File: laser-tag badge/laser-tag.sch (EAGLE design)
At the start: 47 parts, among them J1 JUMPER_SOLDER_1X2_CLOSED, J2 JUMPER_SOLDER_1X2_OPEN, J3 JUMPER_SOLDER_1X2_CLOSED, J4 JUMPER_SOLDER_1X2_CLOSED, J5 JUMPER_SOLDER_1X2_CLOSED, P1 E1260CS021, U1 MKL27Z256VLH4

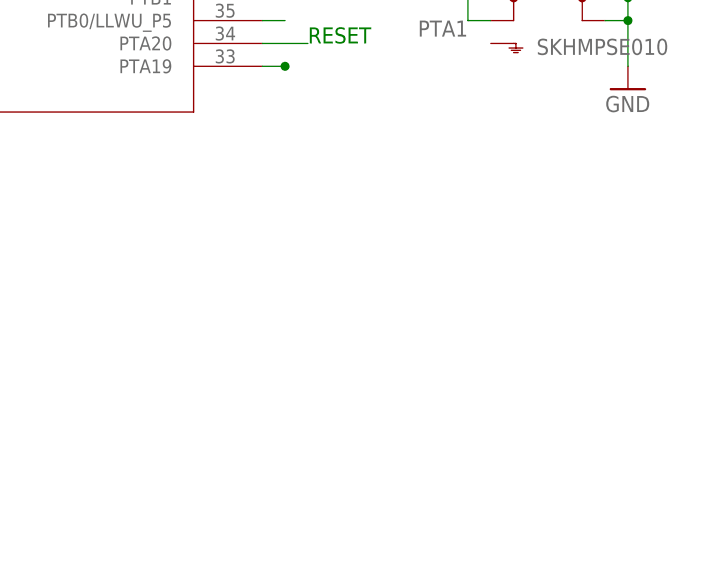
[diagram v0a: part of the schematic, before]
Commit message: Added fiducials
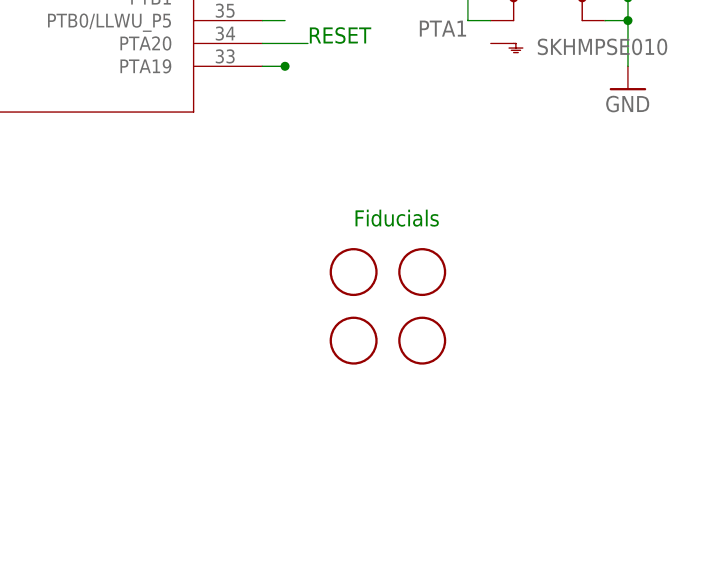
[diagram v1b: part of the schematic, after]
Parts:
- added U$1, U$2, U$3, U$4: FIDUCIAL, adafruit:FIDUCIAL
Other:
- note added: "Fiducials"
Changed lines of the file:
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@@
 <part name="BAT2" library="adafruit" deviceset="CR2032" device="SMT" value="BK-883"/>
 <part name="USB" library="SparkFun-Connectors" deviceset="USB" device="-MICROB" value="10104110-0001LF"/>
+<part name="U$1" library="adafruit" deviceset="FIDUCIAL" device=""/>
+<part name="U$2" library="adafruit" deviceset="FIDUCIAL" device=""/>
+<part name="U$3" library="adafruit" deviceset="FIDUCIAL" device=""/>
+<part name="U$4" library="adafruit" deviceset="FIDUCIAL" device=""/>
 </parts>
 <sheets>
@@
 <text x="-7.62" y="38.1" size="1.778" layer="91">SWD_DIO</text>
 <text x="121.92" y="22.86" size="1.778" layer="91">RESET</text>
+<text x="127" y="2.54" size="1.778" layer="91">Fiducials</text>
 </plain>
 <instances>
@@
 <instance part="BAT2" gate="G$1" x="-124.46" y="88.9" rot="R90"/>
 <instance part="USB" gate="G$1" x="-104.14" y="10.16" rot="R180"/>
+<instance part="U$1" gate="G$1" x="127" y="-2.54"/>
+<instance part="U$2" gate="G$1" x="134.62" y="-2.54"/>
+<instance part="U$3" gate="G$1" x="127" y="-10.16"/>
+<instance part="U$4" gate="G$1" x="134.62" y="-10.16"/>
 </instances>
 <busses>

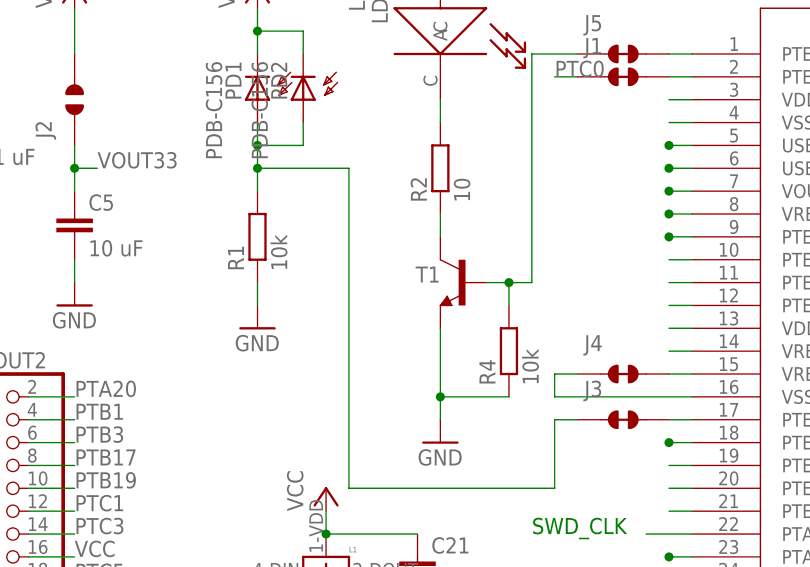
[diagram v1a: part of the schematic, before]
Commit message: Replace T1 with Q1
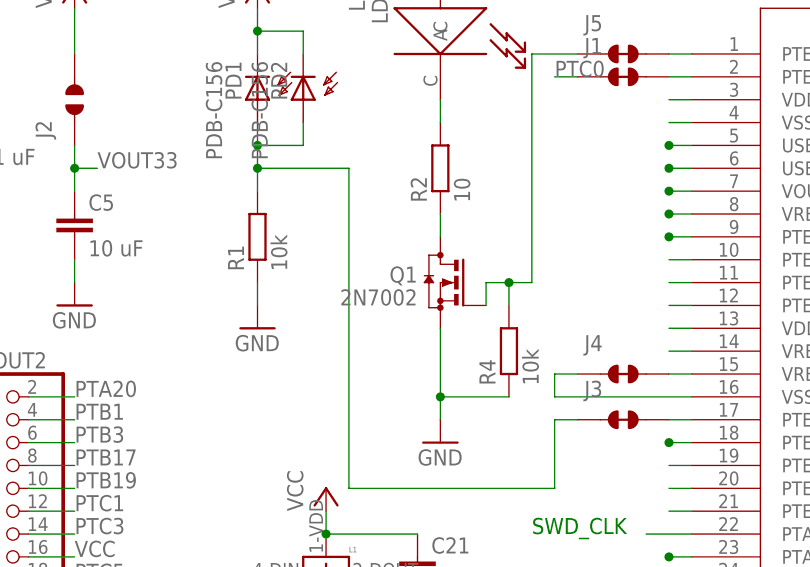
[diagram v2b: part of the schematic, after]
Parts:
- removed T1: (no value), transistor:BC850-NPN-SOT23-BEC
- added Q1: 2N7002, transistor-small-signal:BSS123
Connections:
- net GND: now also Q1.S; no longer T1.E
- net N$1: now also Q1.D; no longer T1.C
- net N$10: now also Q1.G; no longer T1.B
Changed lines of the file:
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@@
 <part name="LD1" library="Photonics" deviceset="LD" device=""/>
 <part name="P+1" library="supply1" deviceset="VCC" device=""/>
-<part name="T1" library="transistor" deviceset="*-NPN-" device="SOT23-BEC" technology="BC850"/>
 <part name="GND1" library="supply1" deviceset="GND" device=""/>
 <part name="P+2" library="supply1" deviceset="VCC" device=""/>
@@
 <part name="U$3" library="adafruit" deviceset="FIDUCIAL" device=""/>
 <part name="U$4" library="adafruit" deviceset="FIDUCIAL" device=""/>
+<part name="Q1" library="transistor-small-signal" deviceset="BSS123" device="" value="2N7002"/>
 </parts>
 <sheets>
@@
 <instance part="LD1" gate="A" x="-17.78" y="101.6" rot="R270"/>
 <instance part="P+1" gate="VCC" x="-17.78" y="114.3"/>
-<instance part="T1" gate="G$1" x="-15.24" y="73.66" smashed="yes" rot="MR0">
-<attribute name="NAME" x="-17.78" y="73.66" size="1.778" layer="95" rot="MR0"/>
-<attribute name="VALUE" x="-5.08" y="78.74" size="1.778" layer="96" rot="MR0"/>
-</instance>
 <instance part="GND1" gate="1" x="-17.78" y="55.88"/>
 <instance part="P+2" gate="VCC" x="-38.1" y="106.68"/>
@@
 <instance part="U$3" gate="G$1" x="127" y="-10.16"/>
 <instance part="U$4" gate="G$1" x="134.62" y="-10.16"/>
+<instance part="Q1" gate="G$1" x="-17.78" y="73.66" rot="MR0"/>
 </instances>
 <busses>
@@
 <segment>
 <pinref part="GND1" gate="1" pin="GND"/>
-<pinref part="T1" gate="G$1" pin="E"/>
 <wire x1="-17.78" y1="58.42" x2="-17.78" y2="60.96" width="0.1524" layer="91"/>
 <pinref part="R4" gate="G$1" pin="1"/>
@@
 <wire x1="-10.16" y1="60.96" x2="-17.78" y2="60.96" width="0.1524" layer="91"/>
 <junction x="-17.78" y="60.96"/>
+<pinref part="Q1" gate="G$1" pin="S"/>
 </segment>
 <segment>
@@
 <net name="N$1" class="0">
 <segment>
-<pinref part="T1" gate="G$1" pin="C"/>
 <pinref part="R2" gate="G$1" pin="1"/>
 <wire x1="-17.78" y1="78.74" x2="-17.78" y2="81.28" width="0.1524" layer="91"/>
+<pinref part="Q1" gate="G$1" pin="D"/>
 </segment>
 </net>
@@
 <net name="N$10" class="0">
 <segment>
-<pinref part="T1" gate="G$1" pin="B"/>
 <wire x1="-12.7" y1="73.66" x2="-10.16" y2="73.66" width="0.1524" layer="91"/>
 <wire x1="-10.16" y1="73.66" x2="-7.62" y2="73.66" width="0.1524" layer="91"/>
@@
 <wire x1="-10.16" y1="71.12" x2="-10.16" y2="73.66" width="0.1524" layer="91"/>
 <junction x="-10.16" y="73.66"/>
-</segment>
-</net>
+<pinref part="Q1" gate="G$1" pin="G"/>
+<wire x1="-12.7" y1="71.12" x2="-12.7" y2="73.66" width="0.1524" layer="91"/>
+</segment>
+</net>

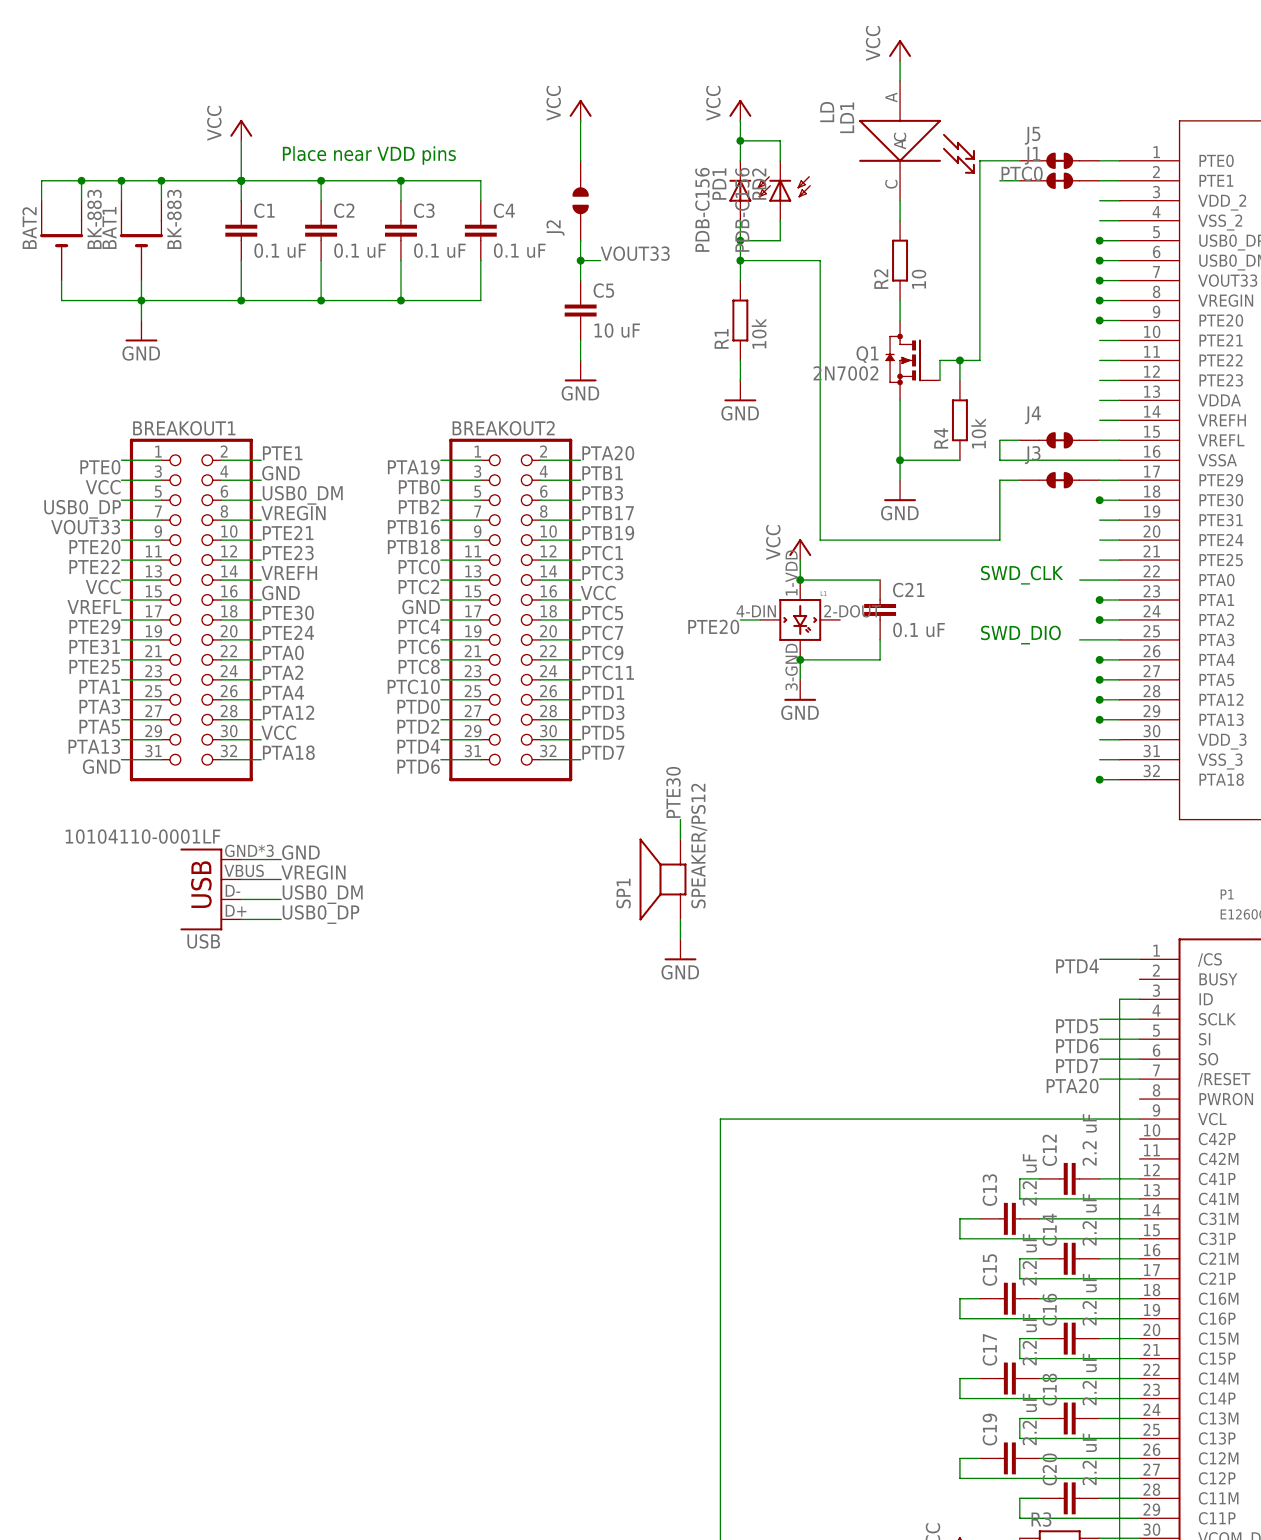
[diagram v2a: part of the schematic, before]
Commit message: Battery protection circuit
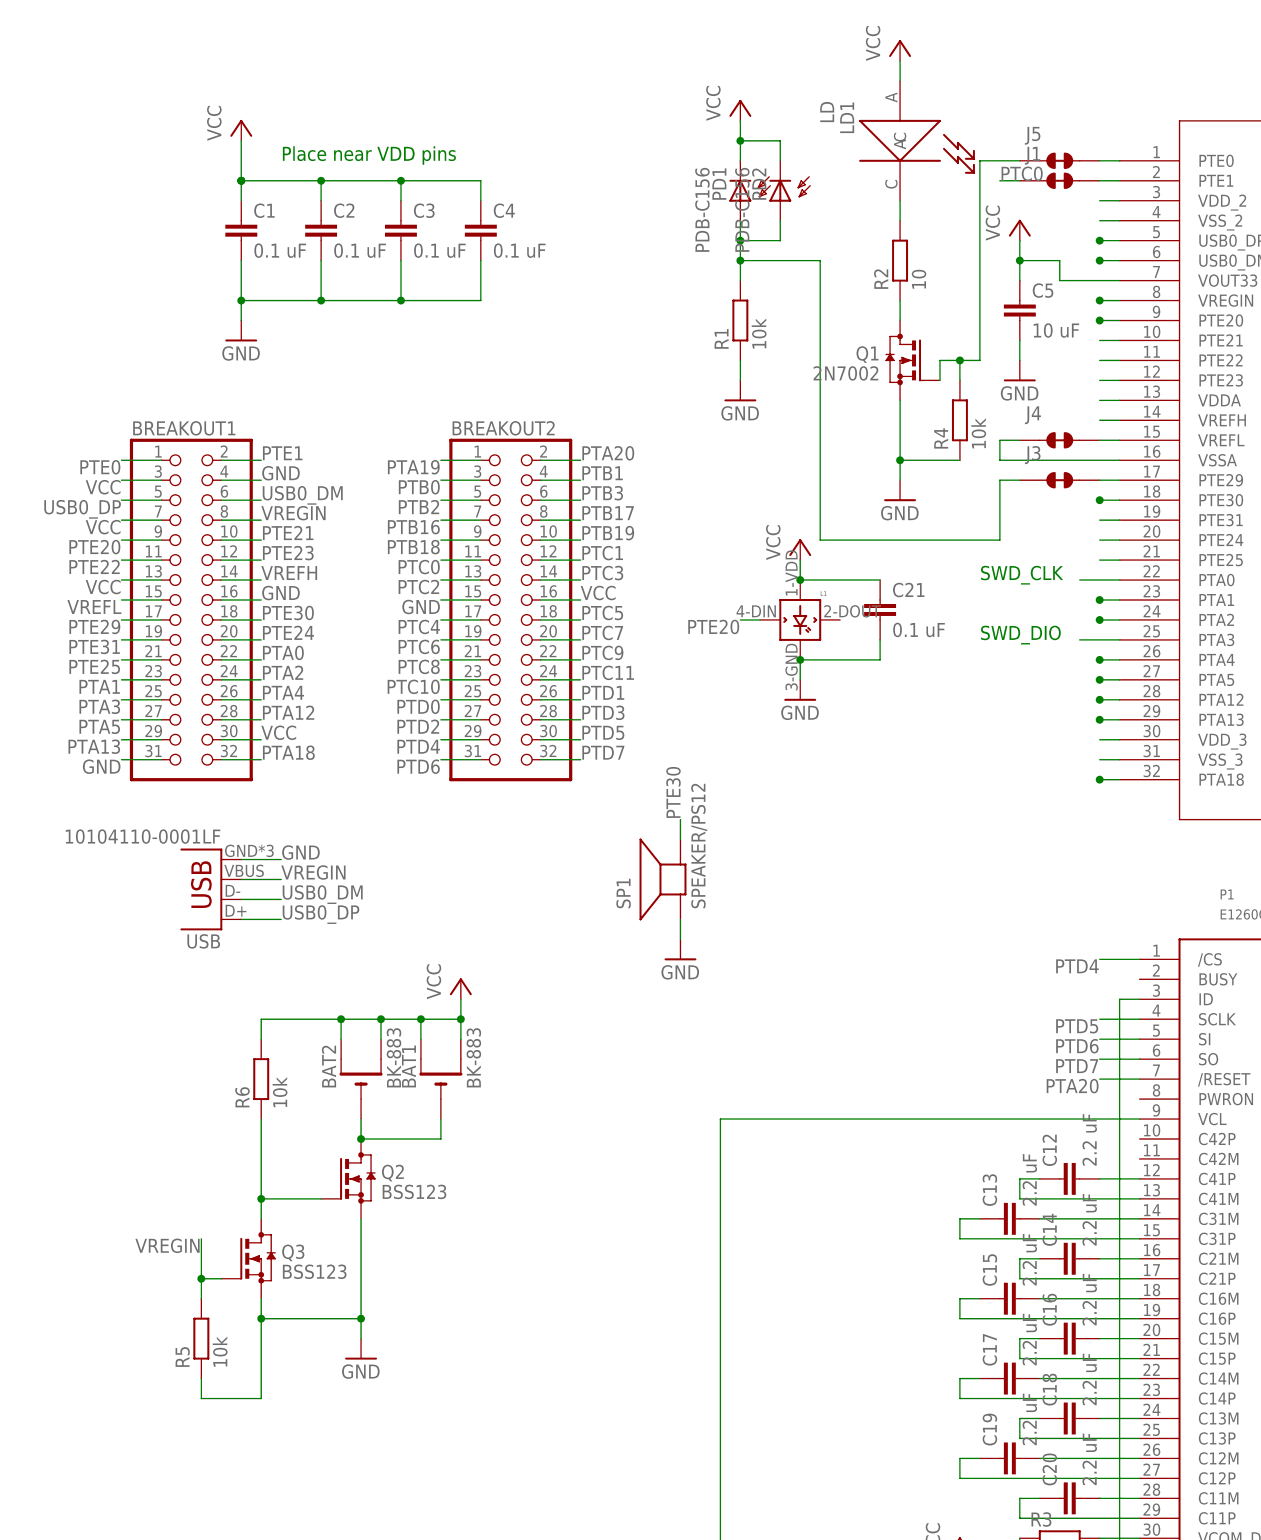
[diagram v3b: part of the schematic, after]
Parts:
- removed J2: JUMPER_SOLDER_1X2_OPEN, Jumpers:JUMPER_SOLDER_1X2_OPEN
- added Q2, Q3: BSS123, transistor-small-signal:BSS123
- added R5, R6: 10k, rcl:R-EU_R0603
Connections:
- removed net VOUT33: BREAKOUT1.7, C5.1, J2.1, U1.VOUT33
- new net N$31: BAT1.-, BAT2.-, Q2.D
- new net N$32: Q2.G, Q3.D, R6.1
- net GND: now also Q2.S, Q3.S, R5.1; no longer BAT1.-, BAT2.-
- net VCC: now also BREAKOUT1.7, C5.1, R6.2, U1.VOUT33; no longer J2.2
- net VREGIN: now also Q3.G, R5.2
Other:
- moved on the sheet: BAT1, BAT2, C5

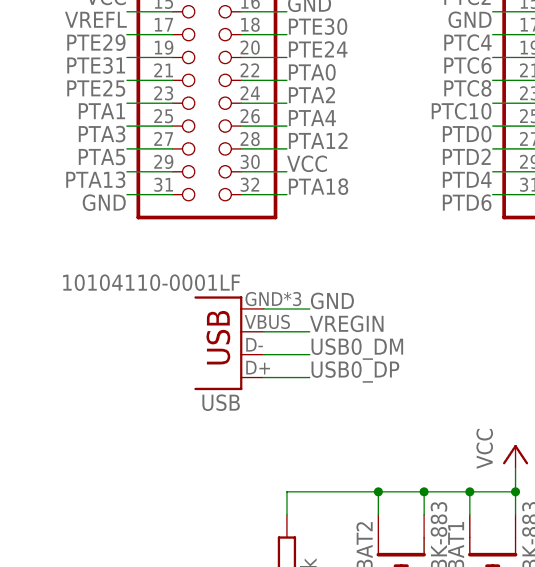
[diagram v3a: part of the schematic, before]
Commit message: Better microUSB connector, v1 on silkscreen
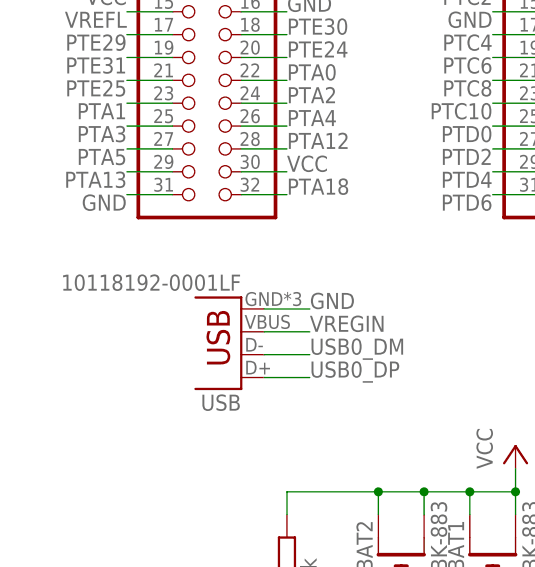
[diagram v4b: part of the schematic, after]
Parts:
- USB: value 10104110-0001LF -> 10118192-0001LF
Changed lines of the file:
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@@
 <part name="R4" library="rcl" deviceset="R-EU_" device="R0603" value="10k"/>
 <part name="BAT2" library="adafruit" deviceset="CR2032" device="SMT" value="BK-883"/>
-<part name="USB" library="SparkFun-Connectors" deviceset="USB" device="-MICROB" value="10104110-0001LF"/>
+<part name="USB" library="SparkFun-Connectors" deviceset="USB" device="-MICROB" value="10118192-0001LF"/>
 <part name="U$1" library="adafruit" deviceset="FIDUCIAL" device=""/>
 <part name="U$2" library="adafruit" deviceset="FIDUCIAL" device=""/>
